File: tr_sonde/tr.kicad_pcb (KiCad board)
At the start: 4 copper layers, 104.4 x 65.3 mm, 87 parts, among them J1 SMA, J2 SMA, J3 SMA, K1 TR, K2 HV_MON, K3 VINHDR, Q1 PBSS4250X, Q2 MMBT2222A, Q3 STD2NK90ZT4, Q4 STD2NK90ZT4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

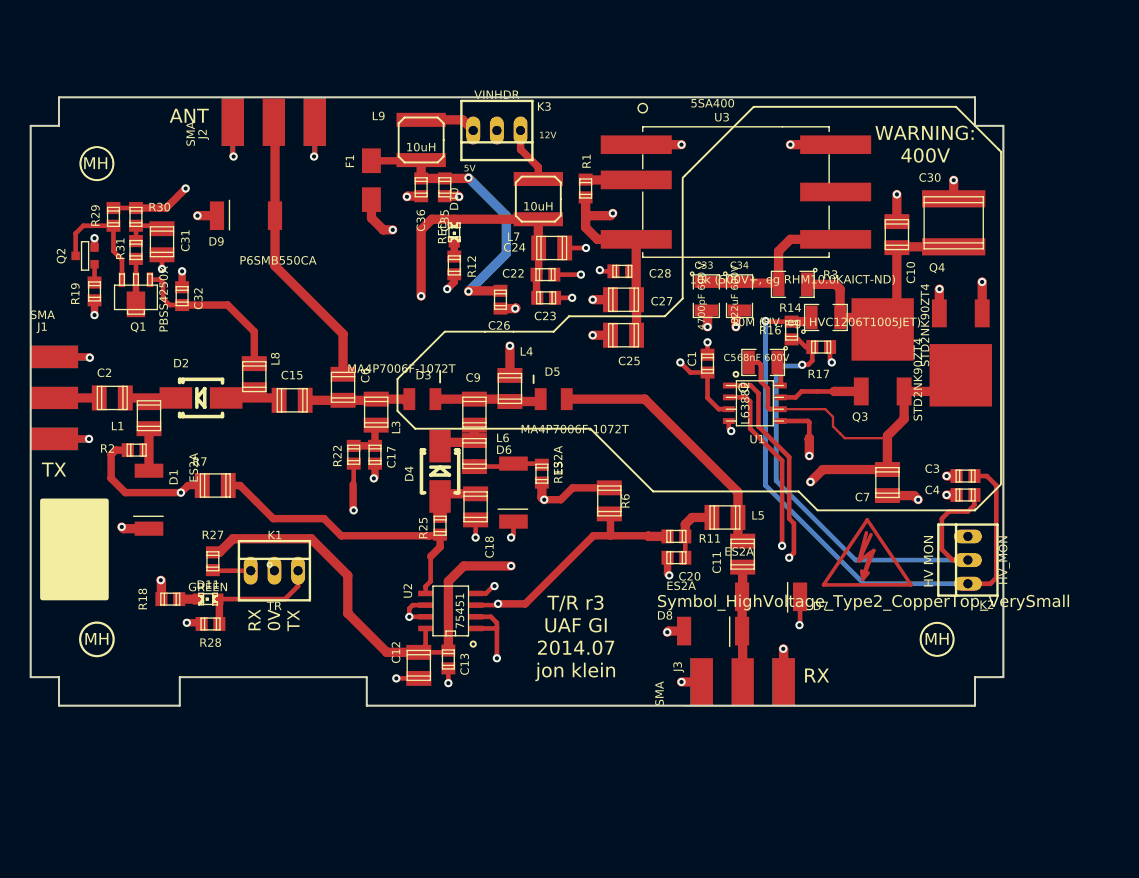
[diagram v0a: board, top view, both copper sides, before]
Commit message: started on t/r with enclosure, migrated distro to 15v
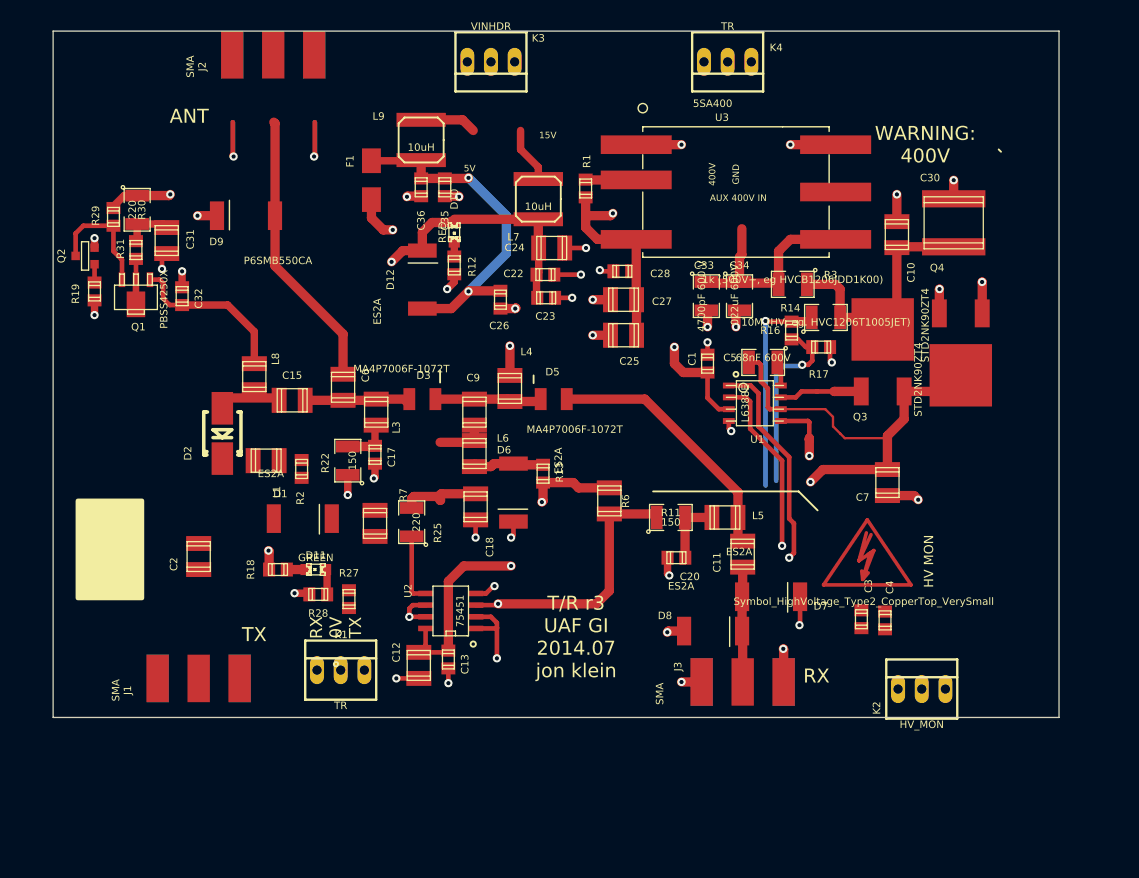
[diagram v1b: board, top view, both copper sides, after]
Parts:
- removed D4: MA4P4006F-1091T, Diodes_SMD:Diode-SMB_Handsoldering
- removed MH (x3): MountingHole_3-5mm_RevA_Date21Jun2010, Mounting_Holes:MountingHole_3-5mm
- added D12: ES2A, smb_diode:SMB_DO2144AA, F.Cu at (99.2, 44.5)
- added K4: TR, Connect:PINHEAD1-3, F.Cu at (132.0, 21.1)
- R11, R22, R25, R30: footprint smd_capacitors:c_0805 -> SMD_Packages:SMD-1210
- R3: value 10k (500V+, eg RHM10.0KAICT-ND) -> 1k (500V+, eg HVCB1206JDD1K00)
- moved J1 33.9 mm to (75.2, 87.2), turned to 90 degrees
- moved C2 19.4 mm to (75.2, 74.2), turned to 90 degrees
- moved C3 19.0 mm to (146.3, 80.9), turned to 270 degrees
- moved R2 17.8 mm to (86.2, 64.8), turned to 90 degrees
- moved R7 17.6 mm to (94.1, 70.6), turned to 270 degrees
- moved D1 16.6 mm to (86.4, 70.1), turned to 0 degrees
- moved C4 16.0 mm to (148.8, 81.0), turned to 270 degrees
- moved R27 15.2 mm to (91.3, 78.7)
- moved K2 14.7 mm to (152.8, 88.4), turned to 0 degrees
- moved L1 13.5 mm to (82.4, 63.9), turned to 180 degrees
- moved K1 12.8 mm to (90.4, 86.4)
- moved D11 12.0 mm to (87.8, 75.6)
- moved R18 12.0 mm to (83.7, 75.6)
- moved R28 12.0 mm to (88.0, 78.2)
- moved K3 7.39 mm to (106.6, 21.1)
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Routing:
- net Net-(C3-Pad1): track 64.9 -> 22.8 mm
- net VCC: track 200.2 -> 159.0 mm, vias 5 -> 4
- net /RX: track 108.9 -> 70.4 mm
- net Net-(C4-Pad1): track 55.9 -> 20.0 mm
- net GND: track 123.0 -> 87.6 mm, vias 45 -> 38
- net /TX: track 106.0 -> 76.9 mm
- net /TXDRV: track 32.3 -> 7.53 mm
- net +5V: track 120.2 -> 95.8 mm
- net (no net): track 0.00 -> 15.1 mm, vias 0 -> 2
- net Net-(C2-Pad1): track 10.5 -> 0.00 mm
- net Net-(D1-Pad1): track 9.84 -> 0.00 mm
- net Net-(C33-Pad1): track 17.9 -> 23.7 mm
- net Net-(C2-Pad2): track 4.83 -> 0.00 mm
- net Net-(C18-Pad1): track 6.28 -> 8.65 mm
- net /RXDRV: track 98.3 -> 99.6 mm
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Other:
- board size 104.4 x 65.3 mm -> 108 x 73.7 mm
- board text added: "15V"
- board text added: "400V"
- board text added: "AUX 400V IN"
- board text added: "GND"
- board text removed: "12V"

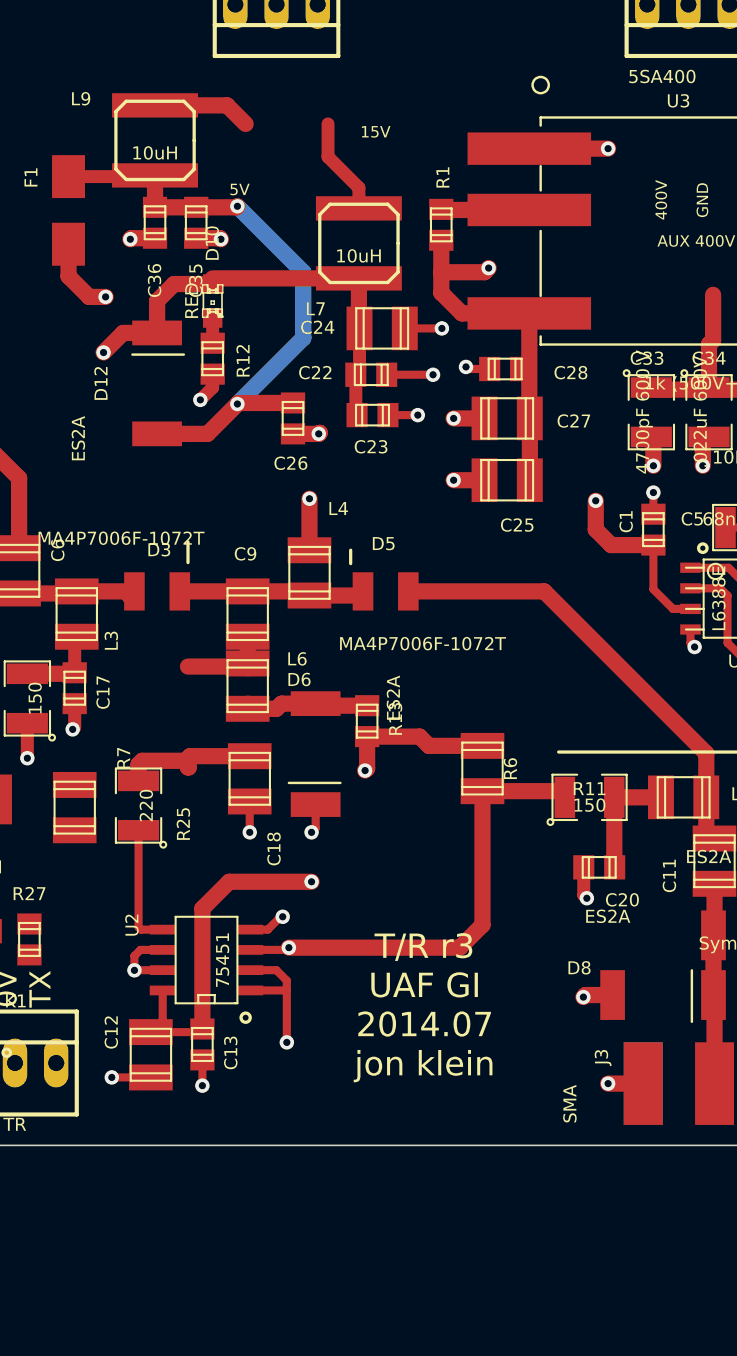
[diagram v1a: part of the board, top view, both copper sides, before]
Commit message: added footprint for smd limiter
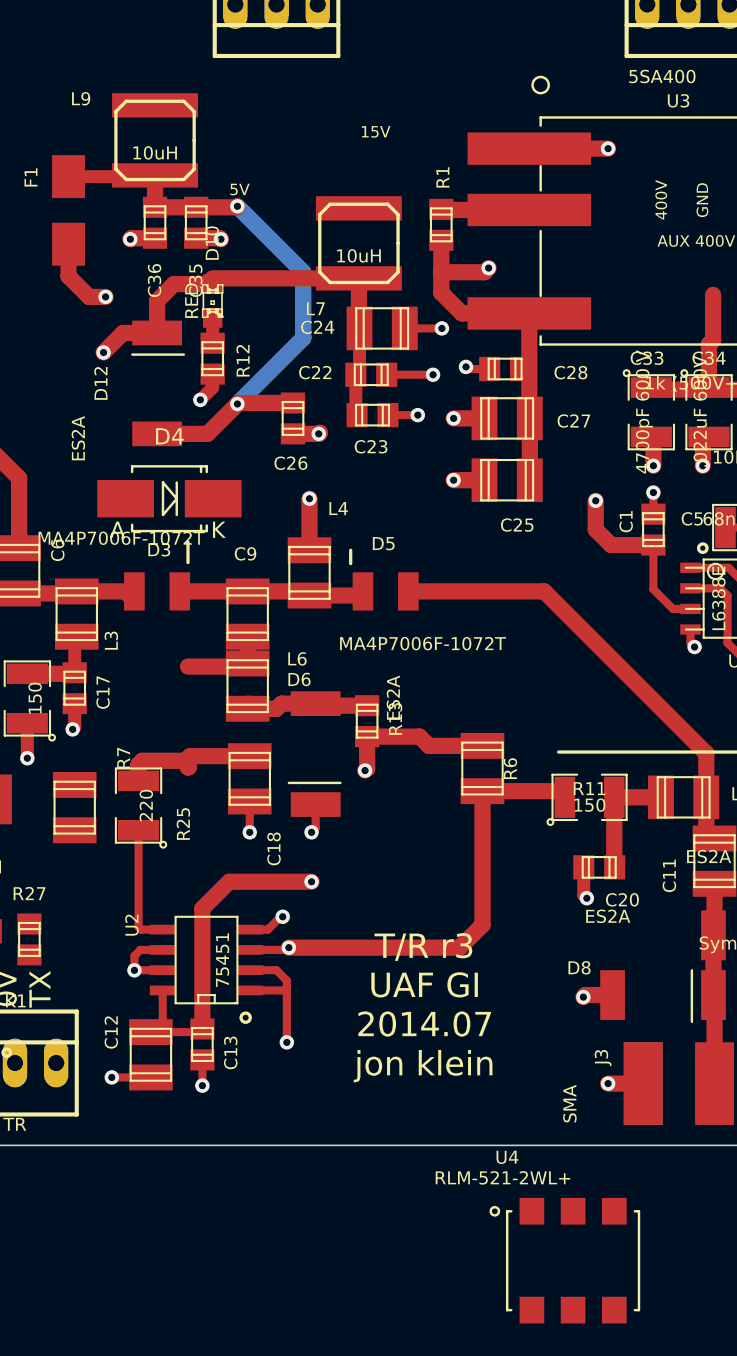
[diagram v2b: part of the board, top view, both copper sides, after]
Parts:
- added D4: MA4P4006F-1091T, Diodes_SMD:Diode-SMB_Handsoldering, F.Cu at (99.9, 51.6)
- added U4: RLM-521-2WL+, sdtransmitter:PL258, F.Cu at (124.8, 98.6)
- R16: value 5k1 -> 3k3
- R17: value 10k -> 15k
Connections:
- J3 pad 1: Net-(C11-Pad2) -> Net-(J3-Pad1)
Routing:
- net Net-(K3-Pad3): track 6.06 -> 0.00 mm
- net Net-(K3-Pad1): track 6.00 -> 0.00 mm

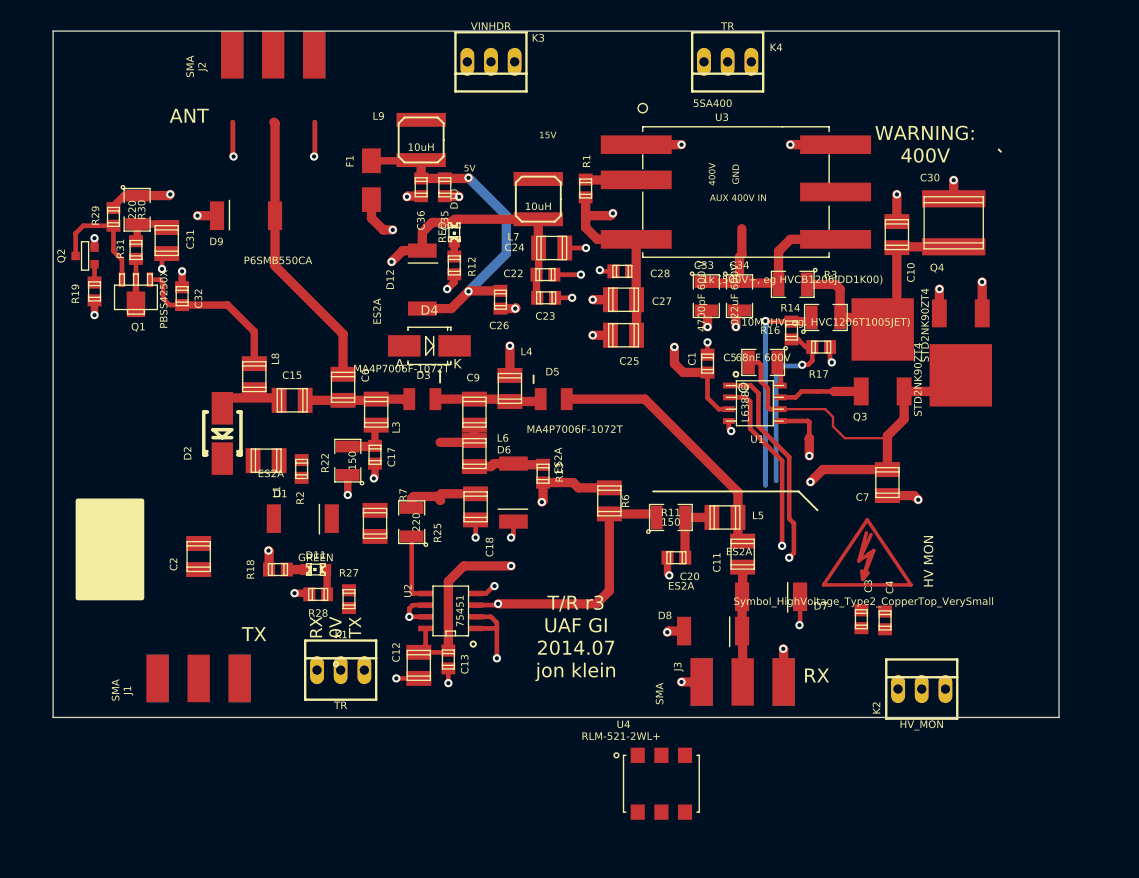
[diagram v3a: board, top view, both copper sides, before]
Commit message: changed all 3 pin headers to molex smd connectors available in tube packaging..
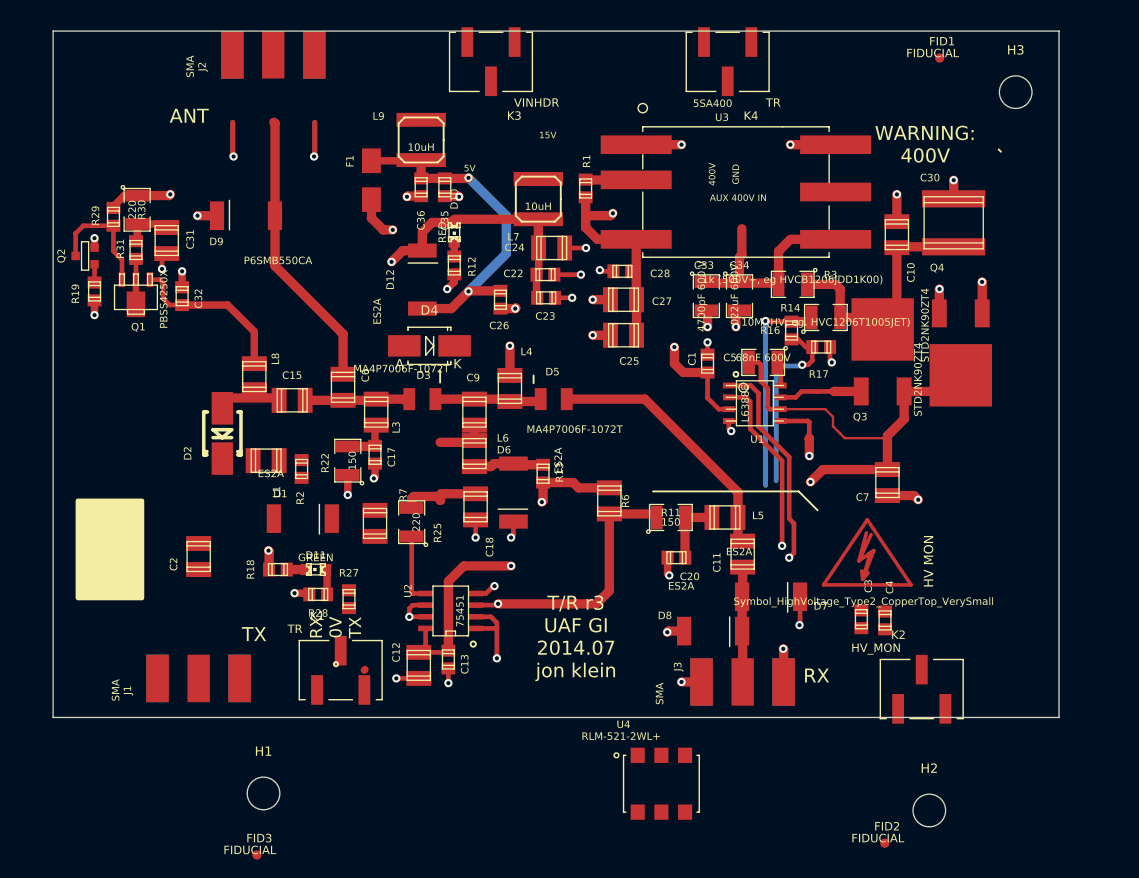
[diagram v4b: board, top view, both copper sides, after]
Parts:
- added FID1: FIDUCIAL, sdtransmitter:FID_1MM, F.Cu at (154.7, 20.7)
- added FID2: FIDUCIAL, sdtransmitter:FID_1MM, F.Cu at (148.8, 104.9)
- added FID3: FIDUCIAL, sdtransmitter:FID_1MM, F.Cu at (81.4, 106.2)
- added H1: MOUNTING_HOLE, Mounting_Holes:MountingHole_3-5mm, F.Cu at (82.1, 99.6)
- added H2: MOUNTING_HOLE, Mounting_Holes:MountingHole_3-5mm, F.Cu at (153.6, 101.4)
- added H3: MOUNTING_HOLE, Mounting_Holes:MountingHole_3-5mm, F.Cu at (162.9, 24.3)
- K1, K2, K3, K4: footprint Connect:PINHEAD1-3 -> sdtransmitter:0740991003

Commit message: rearranged high power T/R switch to place all connectors on one side for easier mounting to cases
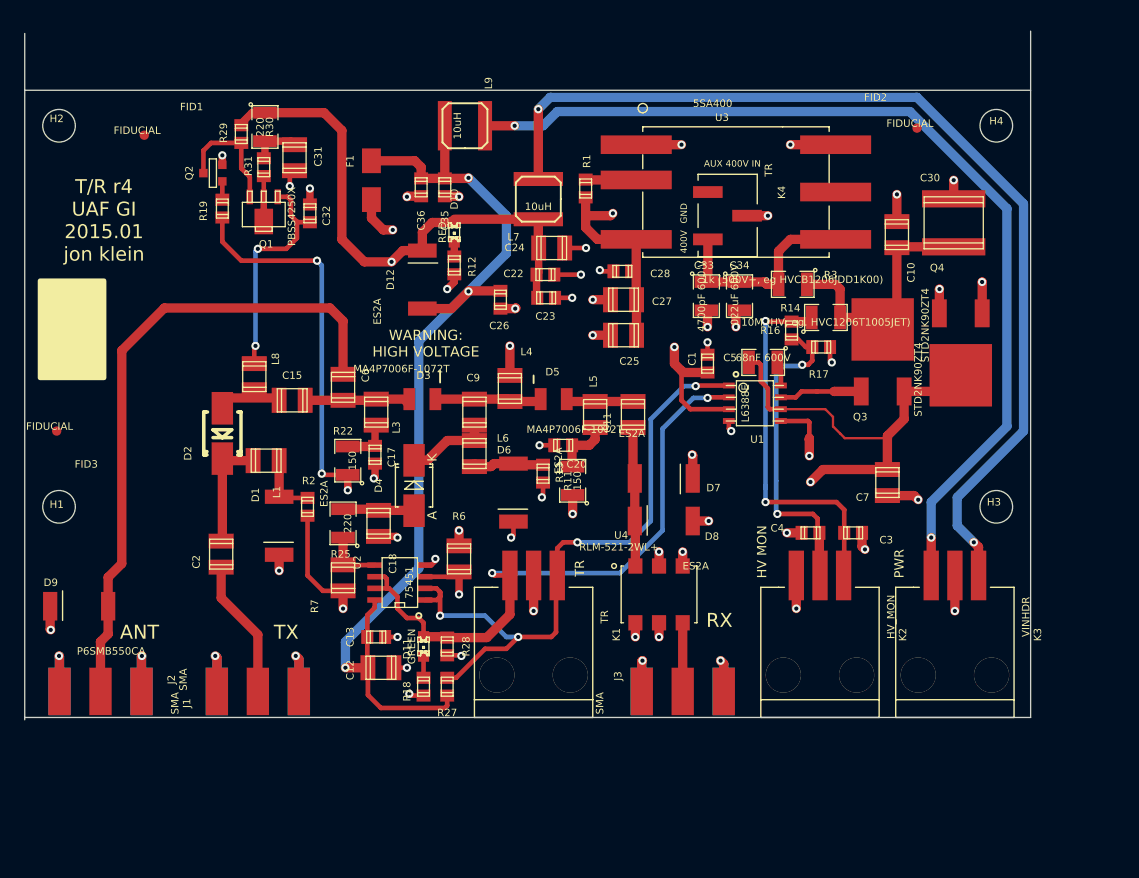
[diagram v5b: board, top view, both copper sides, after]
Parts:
- removed ?: Symbol_HighVoltage_Type2_CopperTop_VerySmall, Footprint_Symbols:Symbol_HighVoltage_Type2_CopperTop_VerySmall
- added H4: MOUNTING_HOLE, Mounting_Holes:MountingHole_3-5mm, F.Cu at (160.8, 27.9)
- K1, K2, K3: footprint sdtransmitter:0740991003 -> sdtransmitter:0015912035
- moved H2 118.8 mm to (60.2, 27.9)
- moved FID1 85.8 mm to (69.3, 29.0)
- moved FID2 76.8 mm to (152.3, 28.2)
- moved K3 74.3 mm to (156.3, 76.2)
- moved J2 70.8 mm to (64.6, 88.6), turned to 270 degrees
- moved FID3 50.3 mm to (59.9, 60.7)
- moved D9 45.6 mm to (62.4, 79.5)
- moved H3 44.5 mm to (160.8, 68.8)
- moved H1 37.8 mm to (60.2, 68.8)
- moved K1 23.1 mm to (111.1, 76.2), turned to 180 degrees
- moved U4 20.3 mm to (124.6, 78.2)
- moved R18 20.1 mm to (99.3, 88.1), turned to 270 degrees
- moved C11 19.1 mm to (121.8, 58.9)
- moved L5 17.8 mm to (117.7, 58.9), turned to 270 degrees
- moved R6 17.3 mm to (103.1, 74.4)
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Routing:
- net Net-(K3-Pad1): track 0.00 -> 108.6 mm, vias 0 -> 2
- net Net-(K3-Pad3): track 0.00 -> 103.7 mm, vias 0 -> 2
- net GND: track 87.6 -> 142.6 mm, vias 38 -> 53
- net Net-(C6-Pad2): track 30.5 -> 69.8 mm
- net VCC: track 159.0 -> 182.7 mm, vias 4 -> 5
- net Net-(C11-Pad1): track 28.0 -> 7.21 mm
- net Net-(C3-Pad1): track 22.8 -> 40.8 mm, vias 1 -> 2
- net +5V: track 95.8 -> 111.4 mm
- net (no net): track 15.2 -> 0.00 mm, vias 2 -> 0
- net Net-(C2-Pad2): track 0.00 -> 15.0 mm
- net Net-(C4-Pad1): track 20.0 -> 34.3 mm, vias 1 -> 2
- net Net-(C2-Pad1): track 0.00 -> 12.3 mm
- net /TX: track 76.8 -> 67.6 mm
- net Net-(J3-Pad1): track 0.00 -> 7.37 mm
- net Net-(D1-Pad1): track 0.00 -> 6.97 mm
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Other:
- board size 108 x 73.7 mm -> 108 x 73.9 mm
- rule trace_min: 0.2 -> 0.18
- board text added: "PWR"
- board text added: "T/R r4 UAF GI 2015.01 jon klein"
- board text added: "TR"
- board text added: "WARNING: HIGH VOLTAGE"
- board text added: "high power T/R switch r4"
- board text removed: "15V"
- board text removed: "5V"
- board text removed: "RX 0V TX"
- board text removed: "T/R r3 UAF GI 2014.07 jon klein"
- board text removed: "WARNING: 400V"
- board text removed: "high power T/R switch r3"

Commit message: cleanups on tr silkscreen, added fault header to driver amp
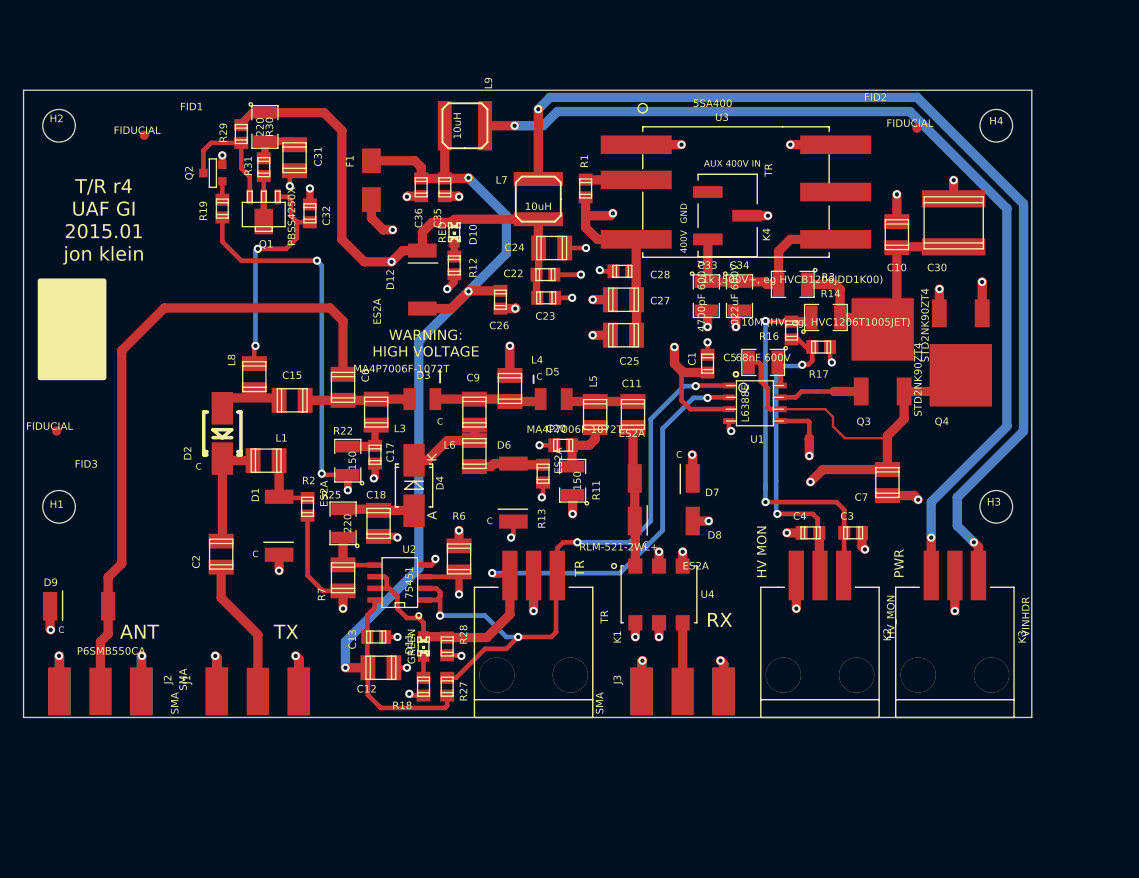
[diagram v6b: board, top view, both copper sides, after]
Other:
- board size 108 x 73.9 mm -> 108.2 x 67.3 mm
- board text added: "C"
